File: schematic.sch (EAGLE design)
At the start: 32 parts, among them IC1 AD8015

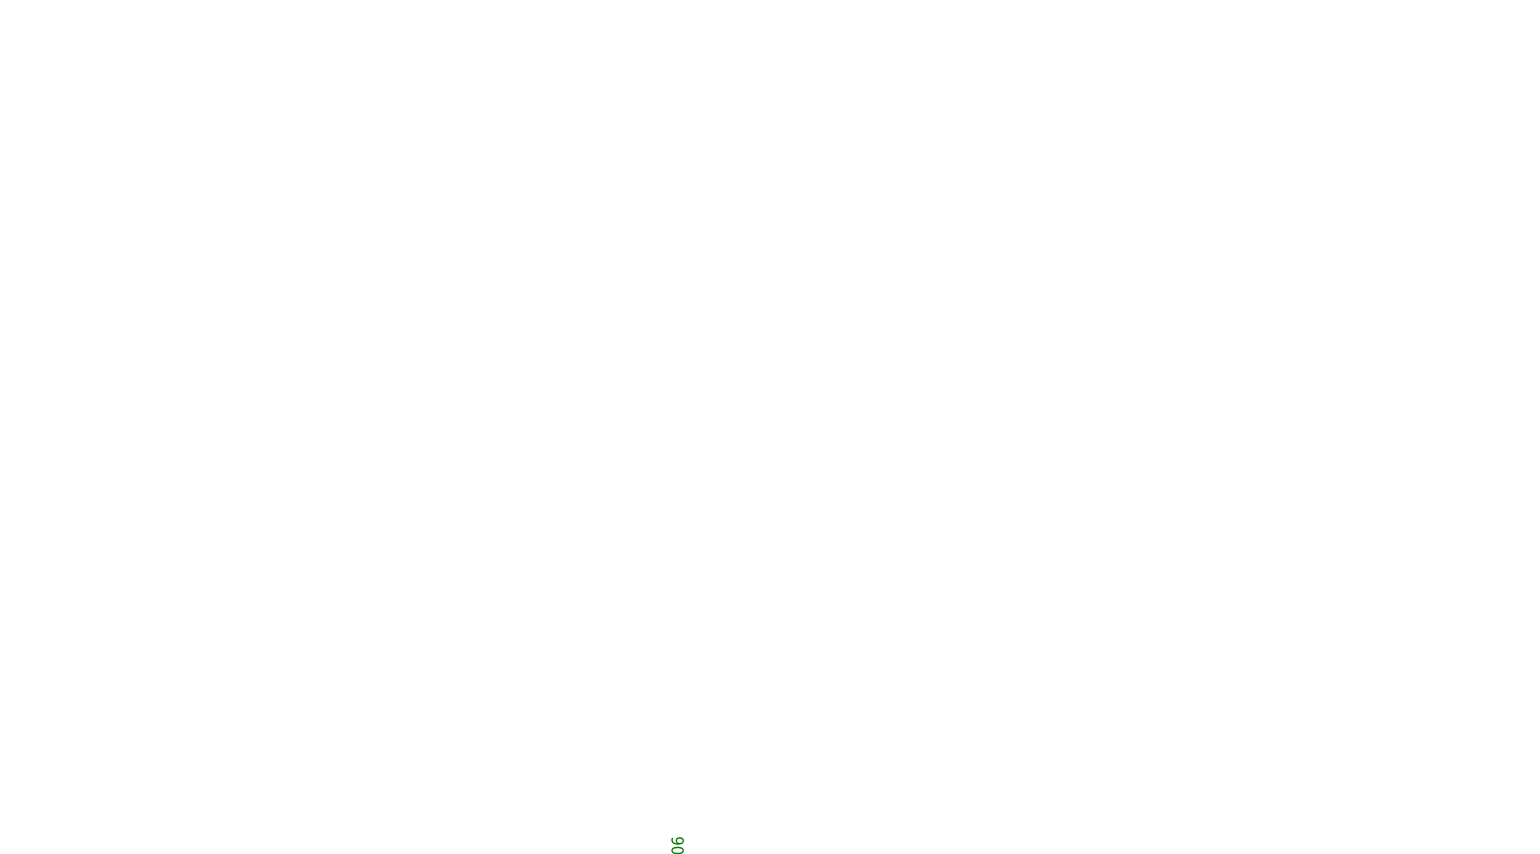
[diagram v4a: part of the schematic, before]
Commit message: Added second channel
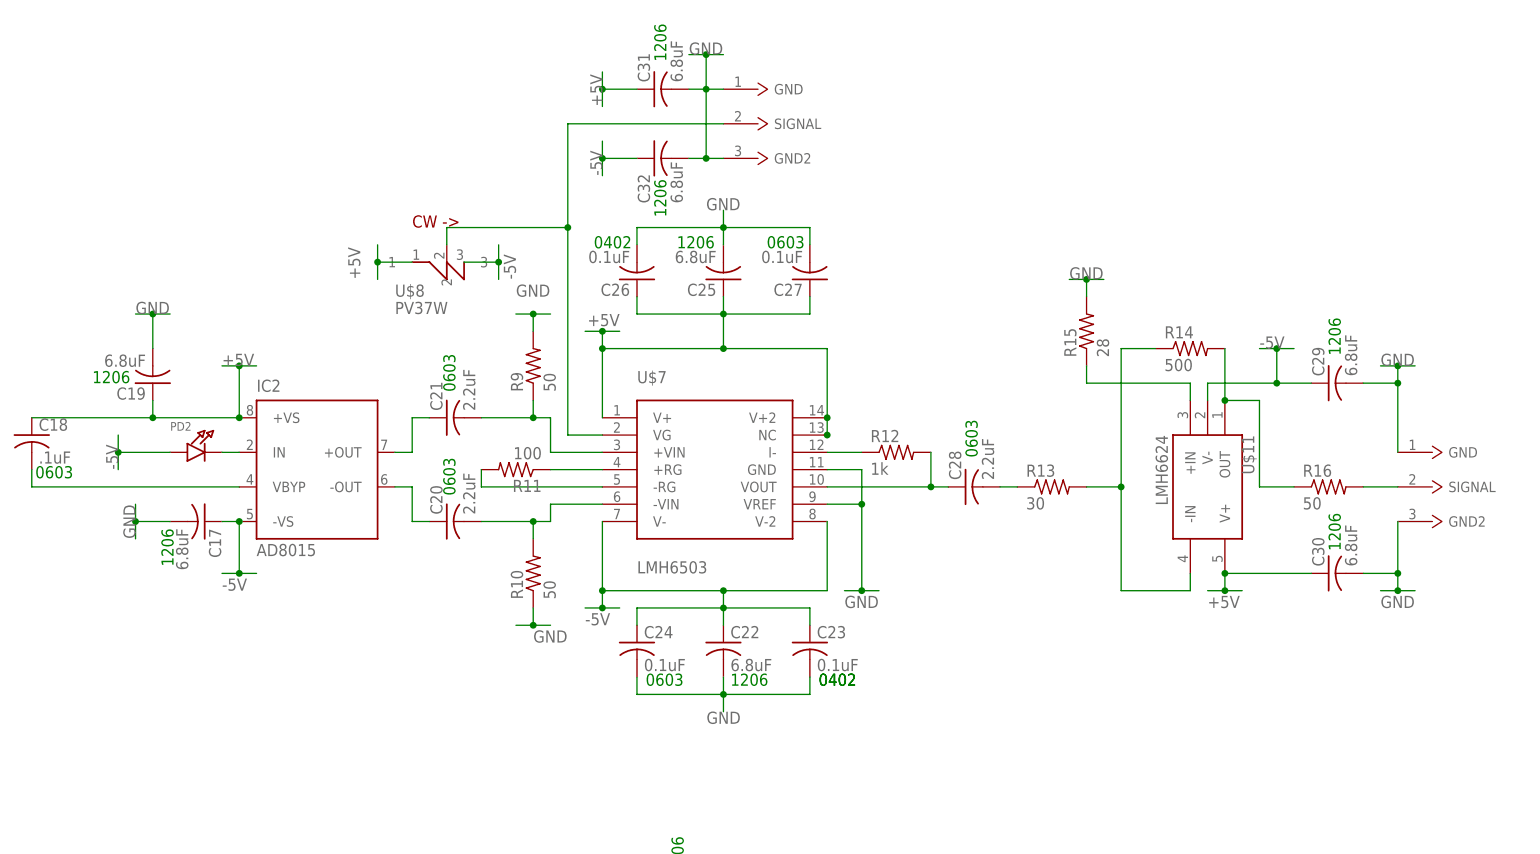
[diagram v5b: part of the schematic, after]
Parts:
- added C17, C19, C22, C25, C29, C30, C31, C32: 6.8uF, rcl:C-USC1206
- added C18: .1uF, rcl:C-USC0603
- added C20, C21, C28: 2.2uF, rcl:C-USC0603
- added C23, C26: 0.1uF, rcl:C-USC0402
- added C24, C27: 0.1uF, rcl:C-USC0603
- added IC2: AD8015, analog-devices:AD8015
- added PD2: (no value), microbuilder:LED1206
- added R10, R16, R9: 50, rcl:R-US_R0603
- added R11: 100, rcl:R-US_R0603
- added R12: 1k, rcl:R-US_R0603
- added R13: 30, rcl:R-US_R0603
- added R14: 500, rcl:R-US_R0603
- added R15: 28, rcl:R-US_R0603
- added U$10, U$9: BNCCONN, 12-ChannelEMG:BNCCONN
- added U$11: LMH6624, 12-ChannelEMG:LMH6624
- added U$7: LMH6503, 12-ChannelEMG:LMH6503
- added U$8: PV37W, 12-ChannelEMG:PV37W
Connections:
- new net N$25: C18.2, IC2.VBYP
- new net N$26: IC2.IN, PD2.C
- new net N$27: C21.1, IC2.+OUT
- new net N$28: C20.1, IC2.-OUT
- new net N$29: C20.2, R10.2, U$7.-VIN
- new net N$30: C21.2, R9.1, U$7.+VIN
- new net N$31: R11.1, U$7.+RG
- new net N$32: R11.2, U$7.-RG
- new net N$33: R12.1, U$7.I-
- new net N$34: C28.1, R12.2, U$7.VOUT
- new net N$35: C28.2, R13.1
- new net N$36: U$7.VG, U$8.2, U$9.SIGNAL
- new net N$37: R13.2, R14.1, U$11.-IN
- new net N$38: R15.1, U$11.+IN
- new net N$39: R14.2, R16.1, U$11.OUT
- new net N$40: R16.2, U$10.SIGNAL
- net +5V: now also C18.1, C19.1, C25.1, C26.1, C27.1, C30.1, C31.1, IC2.+VS, U$11.V+, U$7.NC, U$7.V+, U$7.V+2, U$8.1
- net -5V: now also C17.1, C22.1, C23.1, C24.1, C29.1, C32.1, IC2.-VS, PD2.A, U$11.V-, U$7.V-, U$7.V-2, U$8.3
- net GND: now also C17.2, C19.2, C22.2, C23.2, C24.2, C25.2, C26.2, C27.2, C29.2, C30.2, C31.2, C32.2, R10.1, R15.2, R9.2, U$10.GND, U$10.GND2, U$7.GND, U$7.VREF, U$9.GND, U$9.GND2

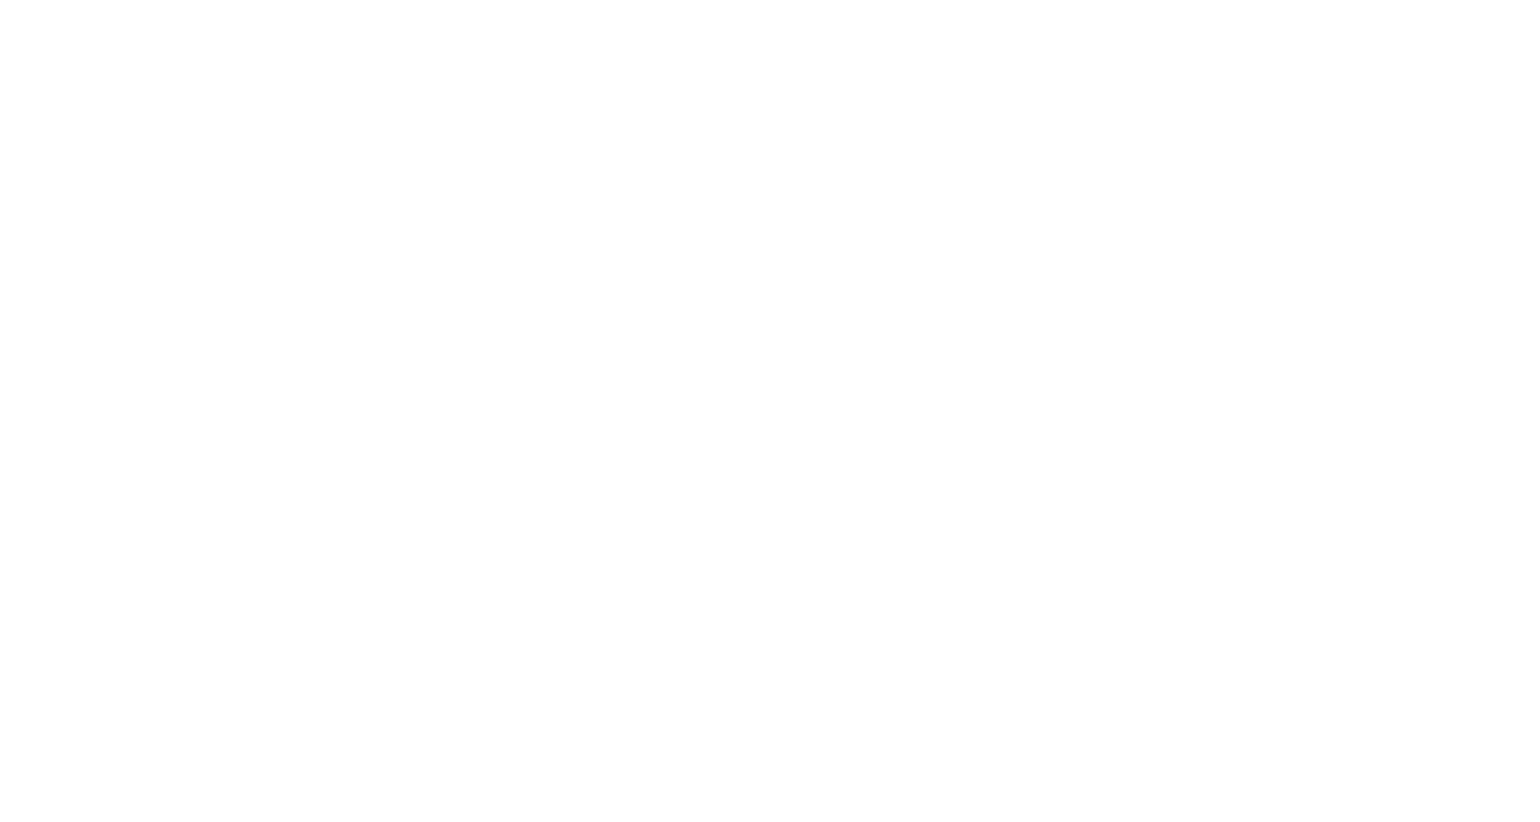
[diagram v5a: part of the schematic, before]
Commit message: Added third channel
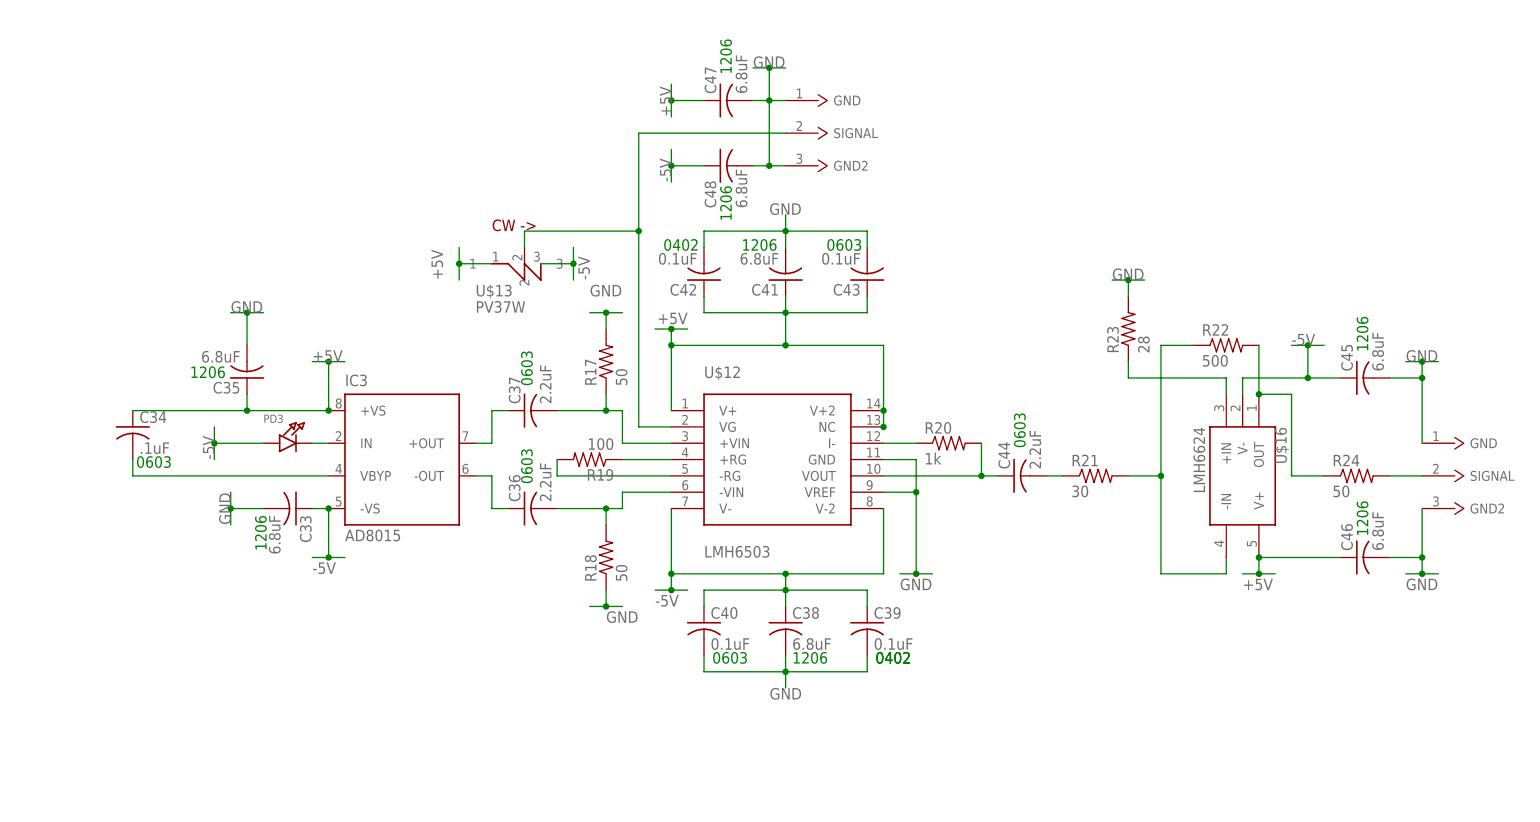
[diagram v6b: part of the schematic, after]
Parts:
- added C33, C35, C38, C41, C45, C46, C47, C48: 6.8uF, rcl:C-USC1206
- added C34: .1uF, rcl:C-USC0603
- added C36, C37, C44: 2.2uF, rcl:C-USC0603
- added C39, C42: 0.1uF, rcl:C-USC0402
- added C40, C43: 0.1uF, rcl:C-USC0603
- added IC3: AD8015, analog-devices:AD8015
- added PD3: (no value), microbuilder:LED1206
- added R17, R18, R24: 50, rcl:R-US_R0603
- added R19: 100, rcl:R-US_R0603
- added R20: 1k, rcl:R-US_R0603
- added R21: 30, rcl:R-US_R0603
- added R22: 500, rcl:R-US_R0603
- added R23: 28, rcl:R-US_R0603
- added U$12: LMH6503, 12-ChannelEMG:LMH6503
- added U$13: PV37W, 12-ChannelEMG:PV37W
- added U$14, U$15: BNCCONN, 12-ChannelEMG:BNCCONN
- added U$16: LMH6624, 12-ChannelEMG:LMH6624
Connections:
- new net N$47: C34.2, IC3.VBYP
- new net N$48: IC3.IN, PD3.C
- new net N$49: C37.1, IC3.+OUT
- new net N$50: C36.1, IC3.-OUT
- new net N$51: C36.2, R18.2, U$12.-VIN
- new net N$52: C37.2, R17.1, U$12.+VIN
- new net N$53: R19.1, U$12.+RG
- new net N$54: R19.2, U$12.-RG
- new net N$55: R20.1, U$12.I-
- new net N$56: C44.1, R20.2, U$12.VOUT
- new net N$57: C44.2, R21.1
- new net N$58: U$12.VG, U$13.2, U$14.SIGNAL
- new net N$59: R21.2, R22.1, U$16.-IN
- new net N$60: R23.1, U$16.+IN
- new net N$61: R22.2, R24.1, U$16.OUT
- new net N$62: R24.2, U$15.SIGNAL
- net +5V: now also C34.1, C35.1, C41.1, C42.1, C43.1, C46.1, C47.1, IC3.+VS, U$12.NC, U$12.V+, U$12.V+2, U$13.1, U$16.V+
- net -5V: now also C33.1, C38.1, C39.1, C40.1, C45.1, C48.1, IC3.-VS, PD3.A, U$12.V-, U$12.V-2, U$13.3, U$16.V-
- net GND: now also C33.2, C35.2, C38.2, C39.2, C40.2, C41.2, C42.2, C43.2, C45.2, C46.2, C47.2, C48.2, R17.2, R18.1, R23.2, U$12.GND, U$12.VREF, U$14.GND, U$14.GND2, U$15.GND, U$15.GND2

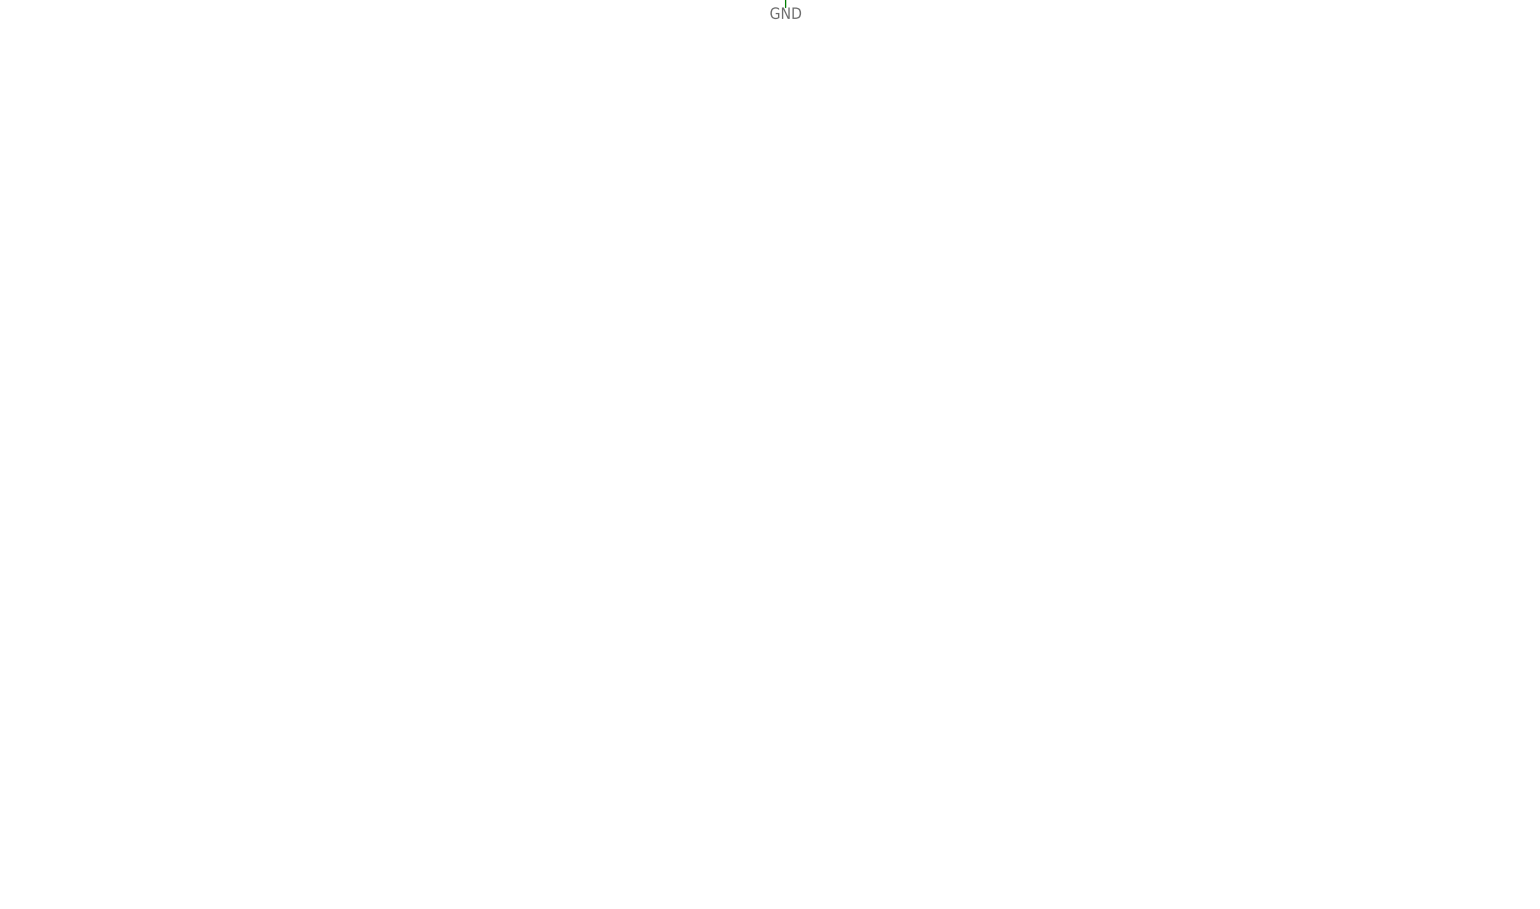
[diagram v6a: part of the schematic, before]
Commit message: Added fourth channel and lined up
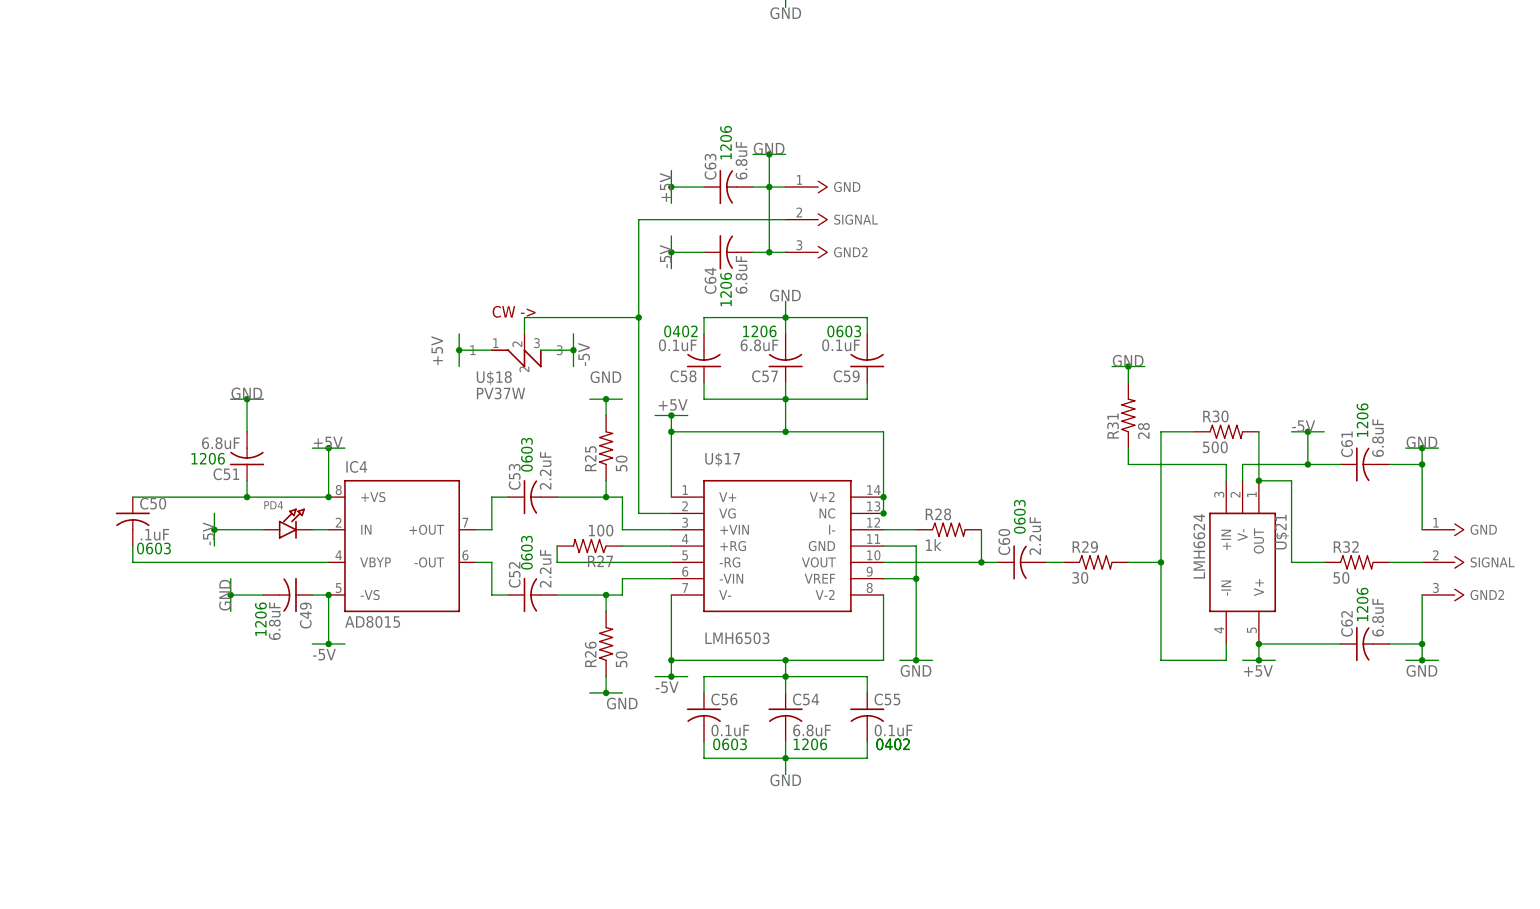
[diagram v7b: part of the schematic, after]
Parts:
- added C49, C51, C54, C57, C61, C62, C63, C64: 6.8uF, rcl:C-USC1206
- added C50: .1uF, rcl:C-USC0603
- added C52, C53, C60: 2.2uF, rcl:C-USC0603
- added C55, C58: 0.1uF, rcl:C-USC0402
- added C56, C59: 0.1uF, rcl:C-USC0603
- added IC4: AD8015, analog-devices:AD8015
- added PD4: (no value), microbuilder:LED1206
- added R25, R26, R32: 50, rcl:R-US_R0603
- added R27: 100, rcl:R-US_R0603
- added R28: 1k, rcl:R-US_R0603
- added R29: 30, rcl:R-US_R0603
- added R30: 500, rcl:R-US_R0603
- added R31: 28, rcl:R-US_R0603
- added U$17: LMH6503, 12-ChannelEMG:LMH6503
- added U$18: PV37W, 12-ChannelEMG:PV37W
- added U$19, U$20: BNCCONN, 12-ChannelEMG:BNCCONN
- added U$21: LMH6624, 12-ChannelEMG:LMH6624
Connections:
- new net N$69: C50.2, IC4.VBYP
- new net N$70: IC4.IN, PD4.C
- new net N$71: C53.1, IC4.+OUT
- new net N$72: C52.1, IC4.-OUT
- new net N$73: C52.2, R26.2, U$17.-VIN
- new net N$74: C53.2, R25.1, U$17.+VIN
- new net N$75: R27.1, U$17.+RG
- new net N$76: R27.2, U$17.-RG
- new net N$77: R28.1, U$17.I-
- new net N$78: C60.1, R28.2, U$17.VOUT
- new net N$79: C60.2, R29.1
- new net N$80: U$17.VG, U$18.2, U$19.SIGNAL
- new net N$81: R29.2, R30.1, U$21.-IN
- new net N$82: R31.1, U$21.+IN
- new net N$83: R30.2, R32.1, U$21.OUT
- new net N$84: R32.2, U$20.SIGNAL
- net +5V: now also C50.1, C51.1, C57.1, C58.1, C59.1, C62.1, C63.1, IC4.+VS, U$17.NC, U$17.V+, U$17.V+2, U$18.1, U$21.V+
- net -5V: now also C49.1, C54.1, C55.1, C56.1, C61.1, C64.1, IC4.-VS, PD4.A, U$17.V-, U$17.V-2, U$18.3, U$21.V-
- net GND: now also C49.2, C51.2, C54.2, C55.2, C56.2, C57.2, C58.2, C59.2, C61.2, C62.2, C63.2, C64.2, R25.2, R26.1, R31.2, U$17.GND, U$17.VREF, U$19.GND, U$19.GND2, U$20.GND, U$20.GND2
